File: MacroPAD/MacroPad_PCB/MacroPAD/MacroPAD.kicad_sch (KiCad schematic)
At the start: 54 parts, among them J1 USB_C_Receptacle_USB2.0_16P, SW1 SW_Push, SW2 RotaryEncoder, U1 ATmega32U4-A, U2 USB6B1, Y1 Crystal

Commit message: Changing c-type input with differential pairs
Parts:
- added U3: RS3E075ATTB, RS3E075ATTB:TRANS_RRH040P_ROM, symbol RS3E075AT:RS3E075ATTB
- D10: footprint LED_SMD:LED_WS2812B_PLCC4_5.0x5.0mm_P3.2mm -> LED_SMD:LED_WS2812B-Mini_PLCC4_3.5x3.5mm
- R2, R3: footprint Resistor_SMD:R_1206_3216Metric -> Resistor_SMD:R_0603_1608Metric
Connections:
- net D+: now also J1.A6 (D+), J1.B6 (D+), U2.3 (I/O2); no longer R2.1, U2.6 (I/O2)
- net D-: now also J1.A7 (D-), J1.B7 (D-), U2.2 (I/O1); no longer R3.1, U2.7 (I/O1)
- net GND: now also U3.4 (G)
- net VBUS: now also U3.1 (S), U3.2 (S), U3.3 (S); no longer J1.A4 (VBUS), J1.A9 (VBUS), J1.B4 (VBUS), J1.B9 (VBUS)
- net D_N: now reaches U1.3 (D-)
- net D_N: now also R2.2; no longer R3.2
- net D_P: now reaches U1.4 (D+)
- net D_P: now also R3.2; no longer R2.2
- new net: J1.A4 (VBUS), J1.A9 (VBUS), J1.B4 (VBUS), J1.B9 (VBUS), U3.5 (D), U3.6 (D), U3.7 (D), U3.8 (D)
- new net D_OUT+: R3.1, U2.6 (I/O2)
- new net D_OUT-: R2.1, U2.7 (I/O1)
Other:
- note added: "USB-C / Reverse polarity protection / ESD protection IC"
- note removed: "USB-C / USB protection IC"
- moved on the sheet: SW2

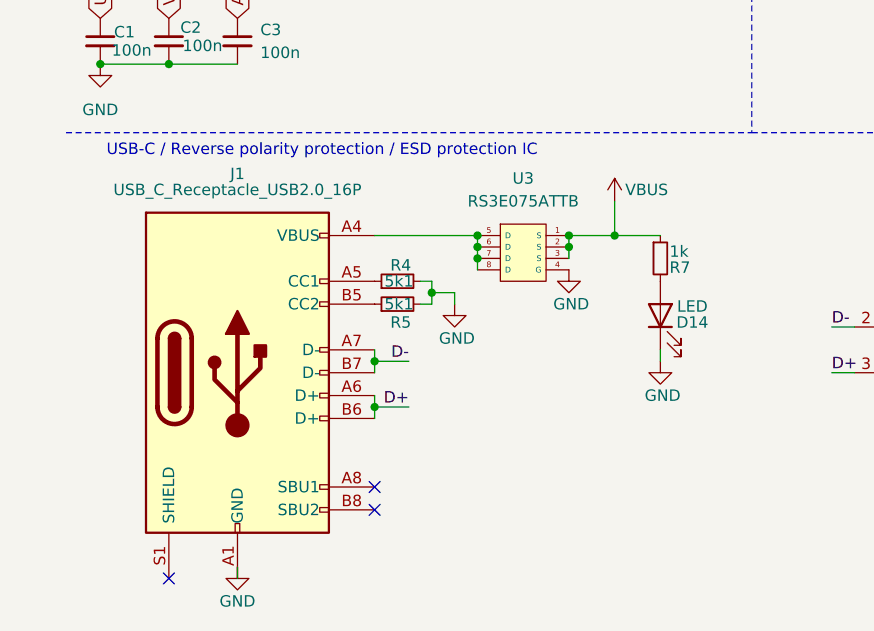
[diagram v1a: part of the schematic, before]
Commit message: Fixed C-type
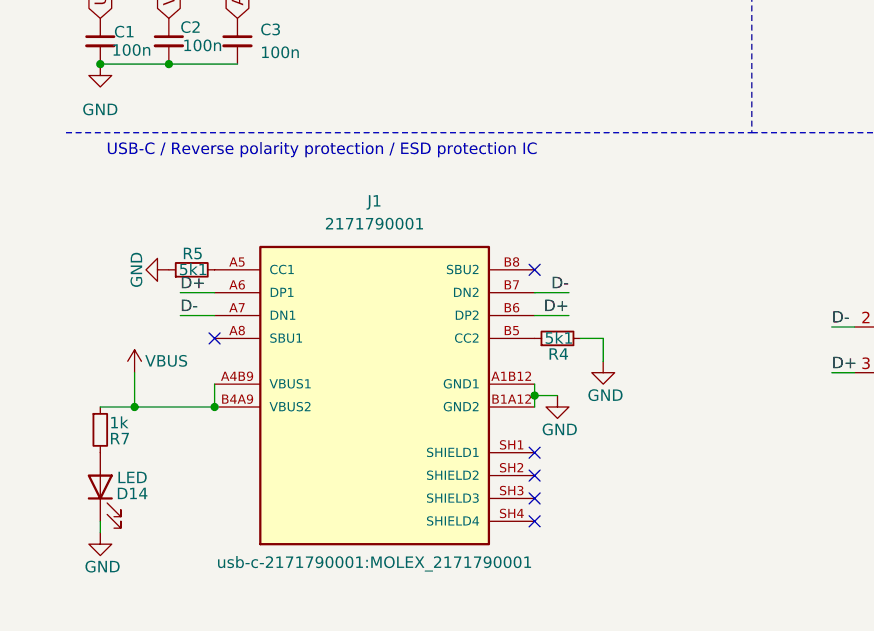
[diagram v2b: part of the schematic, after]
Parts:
- removed J1: USB_C_Receptacle_USB2.0_16P, Connector_USB:USB_C_Receptacle_HRO_TYPE-C-31-M-12, symbol Connector:USB_C_Receptacle_USB2.0_16P
- removed U3: RS3E075ATTB, RS3E075ATTB:TRANS_RRH040P_ROM, symbol RS3E075AT:RS3E075ATTB
- added J1: 2171790001, usb-c-2171790001:MOLEX_2171790001, symbol 2171790001:2171790001
- D10: footprint LED_SMD:LED_WS2812B-Mini_PLCC4_3.5x3.5mm -> LED_SMD:LED_WS2812B_PLCC4_5.0x5.0mm_P3.2mm
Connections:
- net D+: now also J1.A6 (DP1), J1.B6 (DP2)
- net D-: now also J1.A7 (DN1), J1.B7 (DN2)
- net GND: now also R5.1, J1.A1B12 (GND1), J1.B1A12 (GND2); no longer R5.2
- net VBUS: now also J1.A4B9 (VBUS1), J1.B4A9 (VBUS2)
- net at R4.1: now also J1.B5 (CC2)
- new net: J1.A5 (CC1), R5.2
- no-connect marks 17 -> 20
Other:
- moved on the sheet: D14, R7

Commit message: Added ISR Debugg port
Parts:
- added J2: AVR-ISP-6, Connector_IDC:IDC-Header_2x03_P2.54mm_Vertical, symbol Connector:AVR-ISP-6
- D1, D2, D3, D4, D5, D6, D7, D8, D9: value D -> 1N4148
- R4, R5: footprint Resistor_SMD:R_1206_3216Metric -> Resistor_SMD:R_0603_1608Metric
- Y1: value Crystal -> 16MHz
- renumbered J1 to USB-C1
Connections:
- net GND: now also J2.6 (GND)
- net VBUS: now also J2.2 (VCC)
- net ISP_RST: now reaches R1.2, SW1.2, U1.13 (~{RESET})
- net ISP_RST: now also J2.5 (~{RST})
- net MOSI: now reaches U1.10 (PB2)
- net MOSI: now also J2.4 (MOSI)
- net MISO: now reaches U1.11 (PB3)
- net MISO: now also J2.1 (MISO)
- net SCK: now reaches U1.9 (PB1)
- net SCK: now also J2.3 (SCK)
- no-connect marks 20 -> 17
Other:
- note added: "ISP Programmer"
- moved on the sheet: R1, SW2

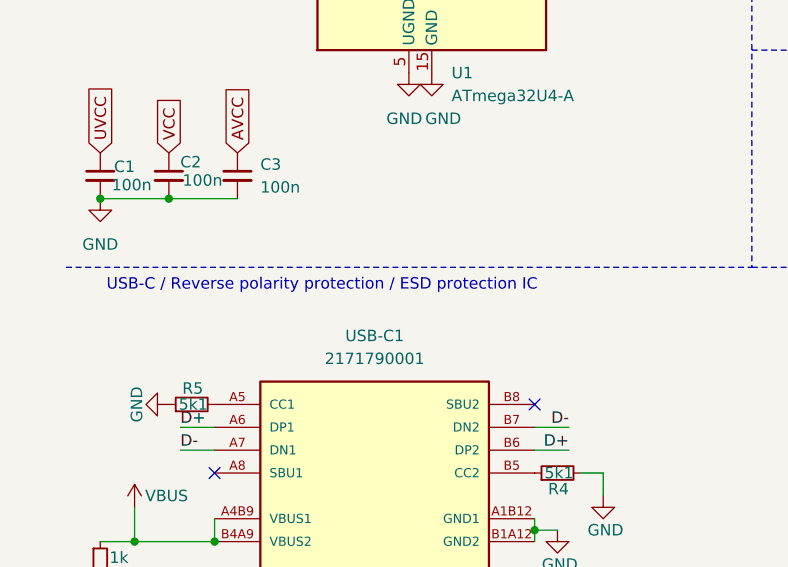
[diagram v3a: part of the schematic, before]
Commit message: Fixed macropad ISR programmer
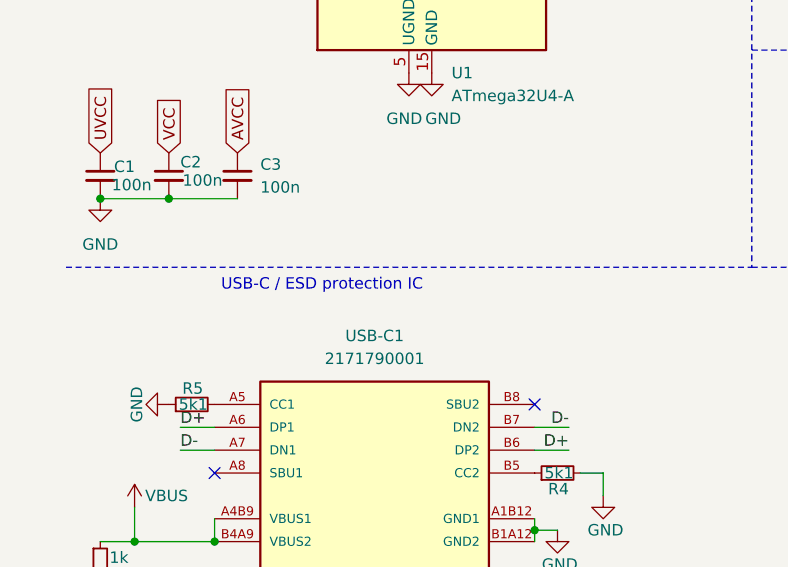
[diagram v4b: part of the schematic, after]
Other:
- note added: "USB-C / ESD protection IC"
- note removed: "USB-C / Reverse polarity protection / ESD protection IC"
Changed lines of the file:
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@@
 		)
 	)
-	(text "USB-C / Reverse polarity protection / ESD protection IC"
+	(text "USB-C / ESD protection IC"
 		(exclude_from_sim no)
 		(at 41.148 144.272 0)
